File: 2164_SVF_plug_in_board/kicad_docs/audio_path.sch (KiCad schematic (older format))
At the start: 24 parts, among them U1 TL072, U2 SSM2164, U3 TL072

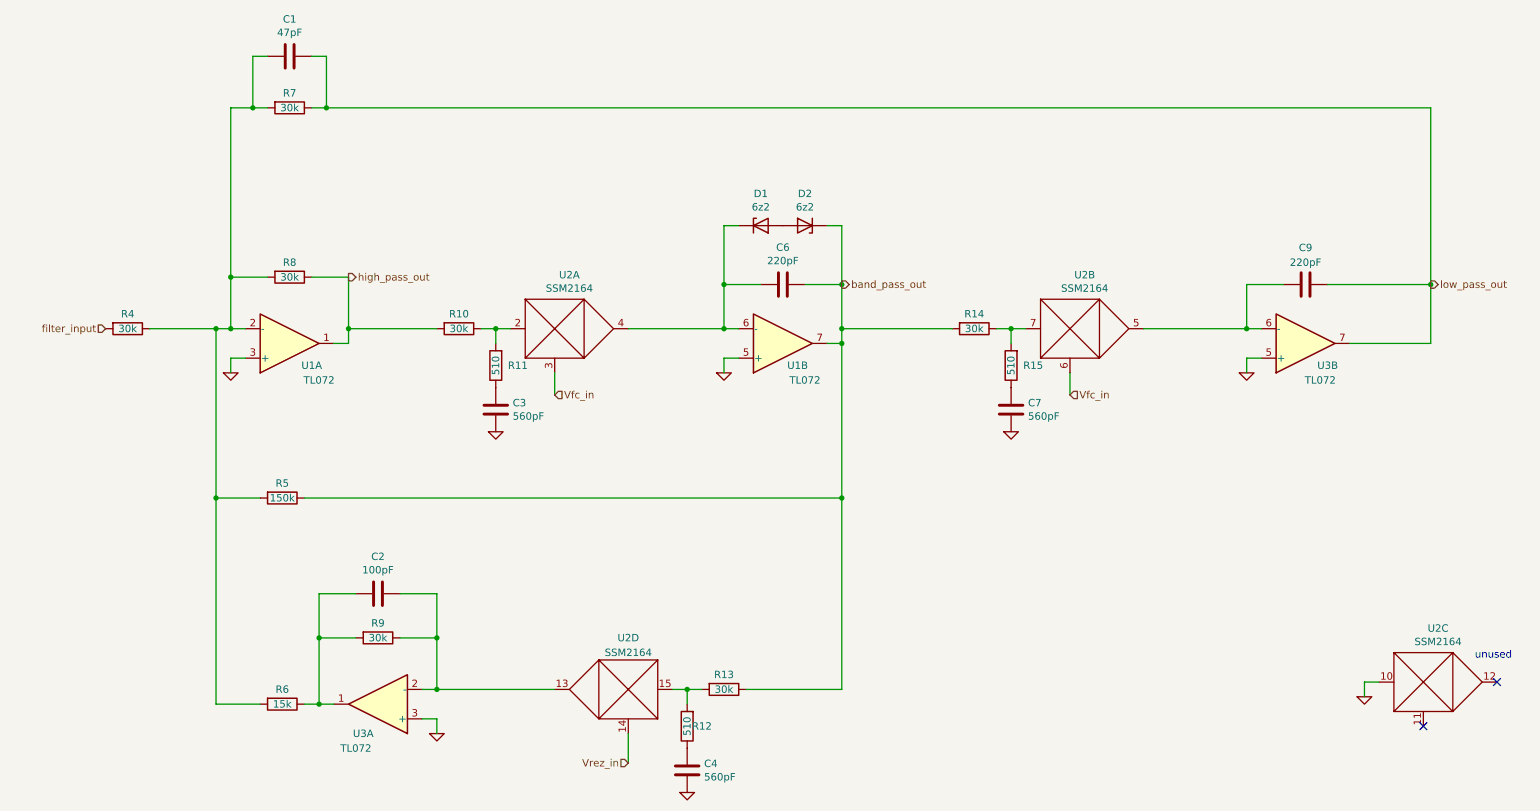
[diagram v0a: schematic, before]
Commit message: change 2164 SVF zeners
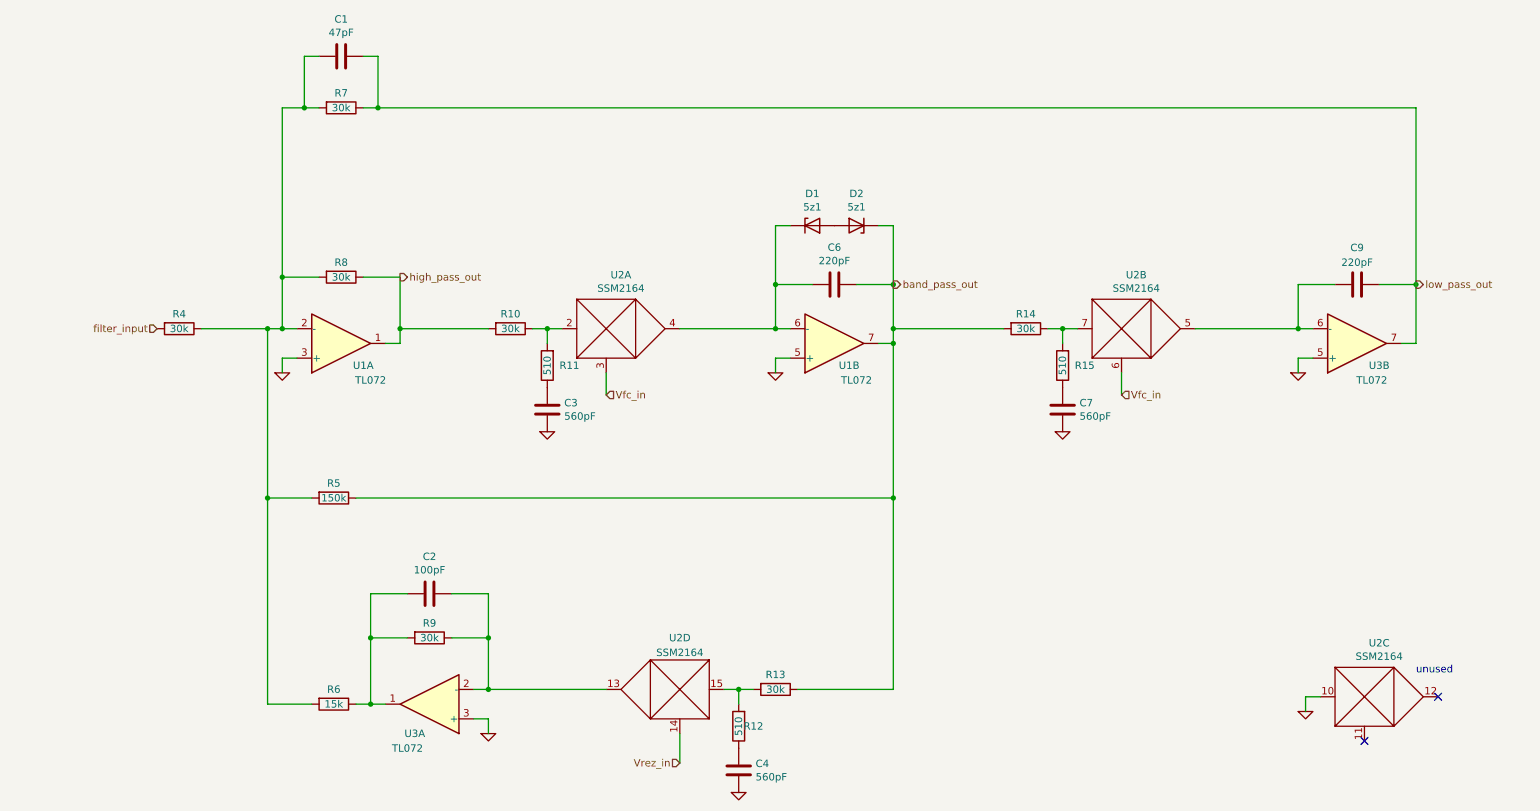
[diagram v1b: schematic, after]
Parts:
- D1, D2: value 6z2 -> 5z1
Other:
- moved on the sheet: C1, C2, C3, C4, C6, C7, C9, D1, D2, R10, R11, R12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
